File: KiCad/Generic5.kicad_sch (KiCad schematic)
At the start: 22 parts, among them J2 Conn_01x04, J3 USB-C, U1 ESP32-PICO-MINI-02, U2 FT231XQ, U3 LMR16006+FB

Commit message: New Generic5
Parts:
- added R7, R8: 27R, RevK:R_0603, symbol Device:R
- renumbered C2 to C1, C5 to C2, C6 to C3, C7 to C4, D3 to D1, D5 to D2, J2 to J1, J3 to J2
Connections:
- net B: now also U1.24 (IO4); no longer U1.15 (IO25)
- net D+: now also R8.2; no longer J2.A6 (D+), J2.B6 (D+)
- net D-: now also R7.2; no longer J2.A7 (D-), J2.B7 (D-)
- net G: now also U1.26 (IO20); no longer U1.13 (IO33)
- net IO1: now also U1.27 (IO7); no longer U1.35 (IO21)
- net IO2: now also U1.33 (IO19); no longer U1.34 (IO22)
- net IO3: now also U1.34 (IO22); no longer U1.21 (IO15)
- net IO4: now also U1.35 (IO21); no longer U1.24 (IO4)
- net R: now also U1.28 (IO8); no longer U1.12 (IO32)
- new net: J2.A6 (D+), J2.B6 (D+), R8.1
- new net: J2.A7 (D-), J2.B7 (D-), R7.1
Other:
- moved on the sheet: C2, C3, C4, D1, D2, L1, R1, R2, R3, R4, U1

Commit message: Extra links
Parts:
- added JP1, JP2: Jumper_2_Open, RevK:Pad_1206_0805_Open, symbol Jumper:Jumper_2_Open
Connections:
- net +3V3: now also JP2.1 (A)
- net G: now also U1.28 (IO8); no longer U1.26 (IO20)
- net GND: now also JP1.1 (A)
- net IO1: now also JP1.2 (B)
- net IO2: now also JP2.2 (B)
- net R: now also U1.26 (IO20); no longer U1.28 (IO8)
- no-connect marks 10 -> 18

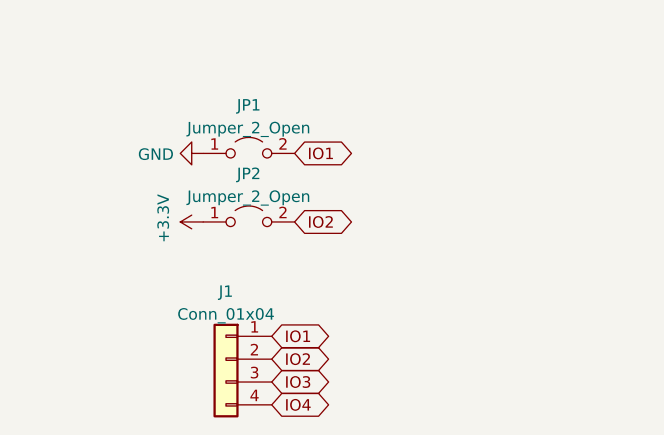
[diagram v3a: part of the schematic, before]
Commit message: New 5V link
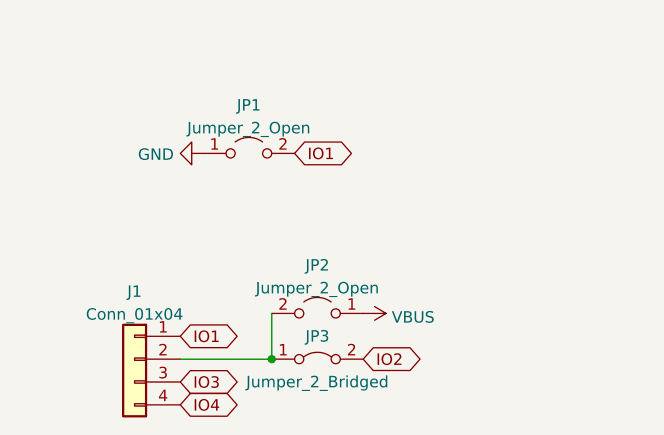
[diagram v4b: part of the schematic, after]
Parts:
- added JP3: Jumper_2_Bridged, RevK:Pad_0603_Bridged, symbol Jumper:Jumper_2_Bridged
- JP1, JP2: footprint RevK:Pad_1206_0805_Open -> RevK:Pad_0603_Open
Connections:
- net +3V3: no longer JP2.1 (A)
- net IO2: now also JP3.2 (B); no longer J1.2 (Pin_2), JP2.2 (B)
- net VBUS: now also JP2.1 (A)
- new net: J1.2 (Pin_2), JP2.2 (B), JP3.1 (A)
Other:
- moved on the sheet: J1, JP2
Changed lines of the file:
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@@
   (junction (at 241.935 134.62) (diameter 0) (color 0 0 0 0)
+  )
+  (junction (at 60.96 154.94) (diameter 0) (color 0 0 0 0)
   )
   (junction (at 205.74 99.06) (diameter 0) (color 0 0 0 0)
@@
     (stroke (width 0) (type default) (color 0 0 0 0))
   )
+  (wire (pts (xy 60.96 149.86) (xy 60.96 154.94))
+    (stroke (width 0) (type default) (color 0 0 0 0))
+  )
   (wire (pts (xy 190.5 99.06) (xy 205.74 99.06))
     (stroke (width 0) (type default) (color 0 0 0 0))
@@
   )
   (wire (pts (xy 190.5 114.3) (xy 187.96 114.3))
+    (stroke (width 0) (type default) (color 0 0 0 0))
+  )
+  (wire (pts (xy 50.8 154.94) (xy 60.96 154.94))
     (stroke (width 0) (type default) (color 0 0 0 0))
   )
@@
     )
   )
-  (global_label "IO3" (shape bidirectional) (at 60.96 157.48 0) (fields_autoplaced)
-    (effects (font (size 1.27 1.27)) (justify left))
-    (property "Intersheet References" "${INTERSHEET_REFS}" (id 0) (at -19.685 115.57 0)
+  (global_label "IO3" (shape bidirectional) (at 50.8 157.48 0) (fields_autoplaced)
+    (effects (font (size 1.27 1.27)) (justify left))
+    (property "Intersheet References" "${INTERSHEET_REFS}" (id 0) (at -29.845 115.57 0)
       (effects (font (size 1.27 1.27)) hide)
     )
@@
     )
   )
-  (global_label "IO2" (shape bidirectional) (at 63.5 139.7 0) (fields_autoplaced)
-    (effects (font (size 1.27 1.27)) (justify left))
-    (property "Intersheet References" "${INTERSHEET_REFS}" (id 0) (at 68.969 139.6206 0)
-      (effects (font (size 1.27 1.27)) (justify left) hide)
-    )
-  )
   (global_label "D+" (shape bidirectional) (at 187.96 116.84 180) (fields_autoplaced)
     (effects (font (size 1.27 1.27)) (justify right))
@@
     )
   )
-  (global_label "IO1" (shape bidirectional) (at 60.96 152.4 0) (fields_autoplaced)
-    (effects (font (size 1.27 1.27)) (justify left))
-    (property "Intersheet References" "${INTERSHEET_REFS}" (id 0) (at -19.685 97.79 0)
-      (effects (font (size 1.27 1.27)) hide)
-    )
-  )
-  (global_label "IO2" (shape bidirectional) (at 60.96 154.94 0) (fields_autoplaced)
-    (effects (font (size 1.27 1.27)) (justify left))
-    (property "Intersheet References" "${INTERSHEET_REFS}" (id 0) (at -19.685 95.25 0)
+  (global_label "IO1" (shape bidirectional) (at 50.8 152.4 0) (fields_autoplaced)
+    (effects (font (size 1.27 1.27)) (justify left))
+    (property "Intersheet References" "${INTERSHEET_REFS}" (id 0) (at -29.845 97.79 0)
+      (effects (font (size 1.27 1.27)) hide)
+    )
+  )
+  (global_label "IO2" (shape bidirectional) (at 71.12 154.94 0) (fields_autoplaced)
+    (effects (font (size 1.27 1.27)) (justify left))
+    (property "Intersheet References" "${INTERSHEET_REFS}" (id 0) (at -9.525 95.25 0)
       (effects (font (size 1.27 1.27)) hide)
     )
@@
     )
   )
-  (global_label "IO4" (shape bidirectional) (at 60.96 160.02 0) (fields_autoplaced)
-    (effects (font (size 1.27 1.27)) (justify left))
-    (property "Intersheet References" "${INTERSHEET_REFS}" (id 0) (at -19.685 74.93 0)
+  (global_label "IO4" (shape bidirectional) (at 50.8 160.02 0) (fields_autoplaced)
+    (effects (font (size 1.27 1.27)) (justify left))
+    (property "Intersheet References" "${INTERSHEET_REFS}" (id 0) (at -29.845 74.93 0)
       (effects (font (size 1.27 1.27)) hide)
     )
@@
     (pin "1")
   )
+  (symbol (lib_id "power:VBUS") (at 71.12 149.86 270) (mirror x) (unit 1)
+    (in_bom yes) (on_board yes) (fields_autoplaced)
+    (property "Reference" "#PWR03" (id 0) (at 67.31 149.86 0)
+      (effects (font (size 1.27 1.27)) hide)
+    )
+    (property "Value" "VBUS" (id 1) (at 74.295 150.2938 90)
+      (effects (font (size 1.27 1.27)) (justify left))
+    )
+    (property "Footprint" "" (id 2) (at 71.12 149.86 0)
+      (effects (font (size 1.27 1.27)) hide)
+    )
+    (property "Datasheet" "" (id 3) (at 71.12 149.86 0)
+      (effects (font (size 1.27 1.27)) hide)
+    )
+    (pin "1")
+  )
   (symbol (lib_id "RevK:FT231XQ") (at 208.28 121.92 0) (unit 1)
     (in_bom yes) (on_board yes) (fields_autoplaced)
@@
     (pin "1")
   )
-  (symbol (lib_id "Jumper:Jumper_2_Open") (at 58.42 139.7 0) (unit 1)
+  (symbol (lib_id "Jumper:Jumper_2_Open") (at 66.04 149.86 0) (mirror y) (unit 1)
     (in_bom no) (on_board yes) (fields_autoplaced)
-    (property "Reference" "JP2" (id 0) (at 58.42 134.3492 0))
-    (property "Value" "Jumper_2_Open" (id 1) (at 58.42 136.8861 0))
-    (property "Footprint" "RevK:Pad_1206_0805_Open" (id 2) (at 58.42 139.7 0)
-      (effects (font (size 1.27 1.27)) hide)
-    )
-    (property "Datasheet" "~" (id 3) (at 58.42 139.7 0)
+    (property "Reference" "JP2" (id 0) (at 66.04 144.5092 0))
+    (property "Value" "Jumper_2_Open" (id 1) (at 66.04 147.0461 0))
+    (property "Footprint" "RevK:Pad_0603_Open" (id 2) (at 66.04 149.86 0)
+      (effects (font (size 1.27 1.27)) hide)
+    )
+    (property "Datasheet" "~" (id 3) (at 66.04 149.86 0)
       (effects (font (size 1.27 1.27)) hide)
     )
@@
     )
     (property "Datasheet" "" (id 3) (at 53.34 132.08 0)
-      (effects (font (size 1.27 1.27)) hide)
-    )
-    (pin "1")
-  )
-  (symbol (lib_id "power:+3.3V") (at 53.34 139.7 90) (unit 1)
-    (in_bom yes) (on_board yes)
-    (property "Reference" "#PWR03" (id 0) (at 57.15 139.7 0)
-      (effects (font (size 1.27 1.27)) hide)
-    )
-    (property "Value" "+3.3V" (id 1) (at 48.9458 139.319 0))
-    (property "Footprint" "" (id 2) (at 53.34 139.7 0)
-      (effects (font (size 1.27 1.27)) hide)
-    )
-    (property "Datasheet" "" (id 3) (at 53.34 139.7 0)
       (effects (font (size 1.27 1.27)) hide)
     )
@@
     (property "Reference" "JP1" (id 0) (at 58.42 126.7292 0))
     (property "Value" "Jumper_2_Open" (id 1) (at 58.42 129.2661 0))
-    (property "Footprint" "RevK:Pad_1206_0805_Open" (id 2) (at 58.42 132.08 0)
+    (property "Footprint" "RevK:Pad_0603_Open" (id 2) (at 58.42 132.08 0)
       (effects (font (size 1.27 1.27)) hide)
     )
@@
     (pin "2")
   )
-  (symbol (lib_id "Connector_Generic:Conn_01x04") (at 55.88 154.94 0) (mirror y) (unit 1)
+  (symbol (lib_id "Connector_Generic:Conn_01x04") (at 45.72 154.94 0) (mirror y) (unit 1)
     (in_bom yes) (on_board yes) (fields_autoplaced)
-    (property "Reference" "J1" (id 0) (at 55.88 147.4302 0))
-    (property "Value" "Conn_01x04" (id 1) (at 55.88 149.9671 0))
-    (property "Footprint" "RevK:Molex_MiniSPOX_H4RA" (id 2) (at 55.88 154.94 0)
-      (effects (font (size 1.27 1.27)) hide)
-    )
-    (property "Datasheet" "~" (id 3) (at 55.88 154.94 0)
+    (property "Reference" "J1" (id 0) (at 45.72 147.4302 0))
+    (property "Value" "Conn_01x04" (id 1) (at 45.72 149.9671 0))
+    (property "Footprint" "RevK:Molex_MiniSPOX_H4RA" (id 2) (at 45.72 154.94 0)
+      (effects (font (size 1.27 1.27)) hide)
+    )
+    (property "Datasheet" "~" (id 3) (at 45.72 154.94 0)
       (effects (font (size 1.27 1.27)) hide)
     )
@@
     (pin "3")
     (pin "4")
+  )
+  (symbol (lib_id "Jumper:Jumper_2_Bridged") (at 66.04 154.94 0) (unit 1)
+    (in_bom no) (on_board yes)
+    (property "Reference" "JP3" (id 0) (at 66.04 152.4 0))
+    (property "Value" "Jumper_2_Bridged" (id 1) (at 66.04 157.48 0))
+    (property "Footprint" "RevK:Pad_0603_Bridged" (id 2) (at 66.04 154.94 0)
+      (effects (font (size 1.27 1.27)) hide)
+    )
+    (property "Datasheet" "~" (id 3) (at 66.04 154.94 0)
+      (effects (font (size 1.27 1.27)) hide)
+    )
+    (pin "1")
+    (pin "2")
   )
   (symbol (lib_id "RevK:LMR16006+FB") (at 231.14 55.88 0) (unit 1)
@@
       (reference "#PWR02") (unit 1) (value "GND") (footprint "")
     )
-    (path "/5efa460e-37f8-4da4-9dd0-46078e47c7b2"
-      (reference "#PWR03") (unit 1) (value "+3.3V") (footprint "")
+    (path "/32f44b1e-28ab-4a81-9817-624dce24101e"
+      (reference "#PWR03") (unit 1) (value "VBUS") (footprint "")
     )
     (path "/00000000-0000-0000-0000-00006046533f"
@@
     )
     (path "/6b6fd764-d949-4699-8423-22321ed8ba1e"
-      (reference "JP1") (unit 1) (value "Jumper_2_Open") (footprint "RevK:Pad_1206_0805_Open")
+      (reference "JP1") (unit 1) (value "Jumper_2_Open") (footprint "RevK:Pad_0603_Open")
     )
     (path "/4c8f85b7-738f-47cd-a8f5-b5d7783c6b06"
-      (reference "JP2") (unit 1) (value "Jumper_2_Open") (footprint "RevK:Pad_1206_0805_Open")
+      (reference "JP2") (unit 1) (value "Jumper_2_Open") (footprint "RevK:Pad_0603_Open")
+    )
+    (path "/c147e8af-96f3-4fd2-9bb9-1b4816490efc"
+      (reference "JP3") (unit 1) (value "Jumper_2_Bridged") (footprint "RevK:Pad_0603_Bridged")
     )
     (path "/00000000-0000-0000-0000-0000610fe01a"

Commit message: Ready for order
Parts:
- added Logo1: AJK, RevK:AJK, symbol RevK:AJK
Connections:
- no-connect marks 18 -> 20
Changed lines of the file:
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@@
   (no_connect (at 73.66 76.2))
   (no_connect (at 226.06 137.16))
+  (no_connect (at 226.06 132.08))
+  (no_connect (at 226.06 129.54))
   (no_connect (at 43.18 81.28))
   (no_connect (at 43.18 73.66))
@@
     (pin "4")
   )
+  (symbol (lib_id "RevK:AJK") (at 276.86 172.72 0) (unit 1)
+    (in_bom no) (on_board yes) (fields_autoplaced)
+    (property "Reference" "Logo1" (id 0) (at 276.86 170.18 0)
+      (effects (font (size 1.27 1.27)) hide)
+    )
+    (property "Value" "AJK" (id 1) (at 277.495 173.1538 0)
+      (effects (font (size 1.27 1.27)) (justify left))
+    )
+    (property "Footprint" "RevK:AJK" (id 2) (at 276.86 175.26 0)
+      (effects (font (size 1.27 1.27)) hide)
+    )
+    (property "Datasheet" "" (id 3) (at 276.86 175.26 0)
+      (effects (font (size 1.27 1.27)) hide)
+    )
+    (property "Note" "Non part, PCB printed" (id 4) (at 276.86 172.72 0)
+      (effects (font (size 1.27 1.27)) hide)
+    )
+  )
   (symbol (lib_id "Jumper:Jumper_2_Bridged") (at 66.04 154.94 0) (unit 1)
     (in_bom no) (on_board yes)
@@
       (reference "L1") (unit 1) (value "6.8uH") (footprint "RevK:Hidden")
     )
+    (path "/a38dd5c8-07fd-48c9-a981-784a5fc4f1d1"
+      (reference "Logo1") (unit 1) (value "AJK") (footprint "RevK:AJK")
+    )
     (path "/3b6e2e43-685e-4e7b-97b9-8f290ca51417"
